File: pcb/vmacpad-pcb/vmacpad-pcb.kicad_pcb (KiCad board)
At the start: 2 copper layers, 134.7 x 126.1 mm, 79 parts, among them J1 TYPE-C-31-M12_13, J2 Conn_01x04_Pin, J3 Conn_01x04_Pin, K1 1u, K10 1u, K12 2.25u, K13 1u, K14 1u, K16 1u, K17 1u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

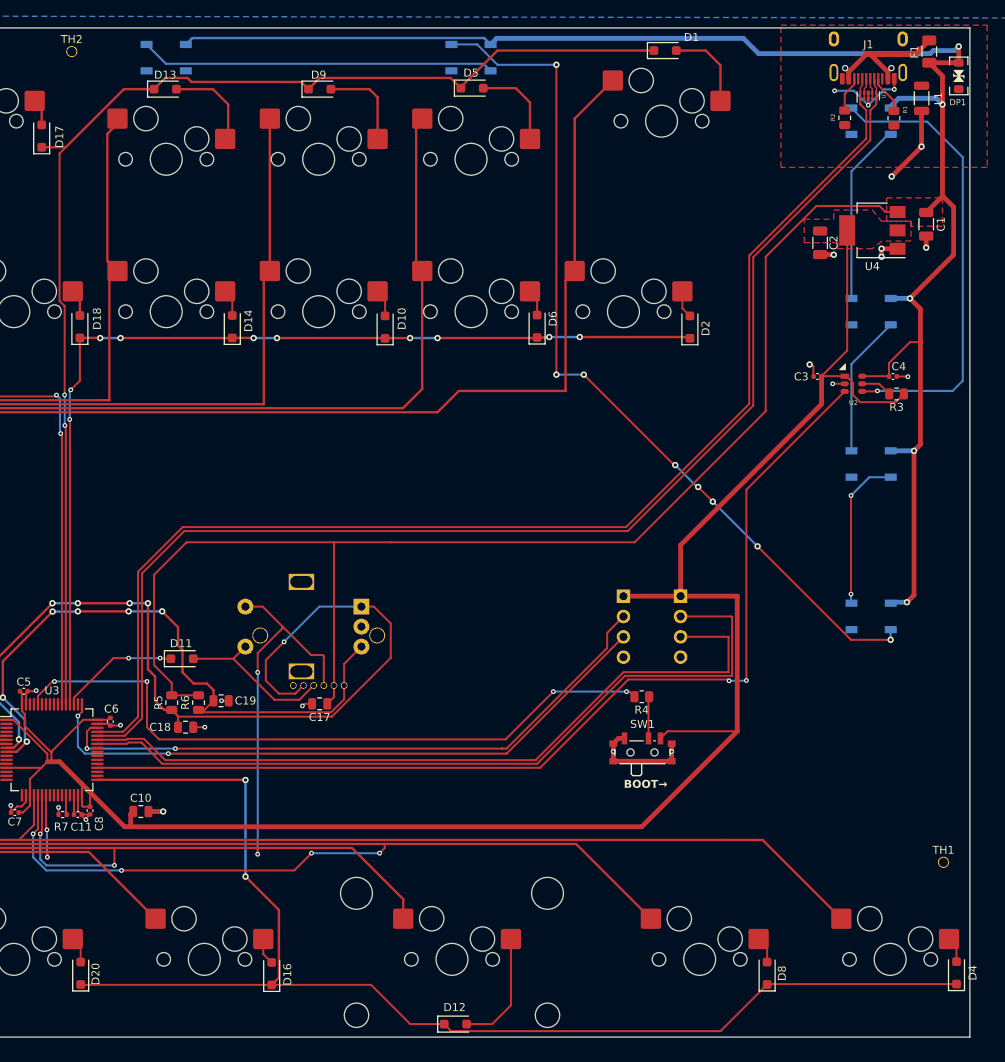
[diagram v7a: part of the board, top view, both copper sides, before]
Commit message: Fix power trace width
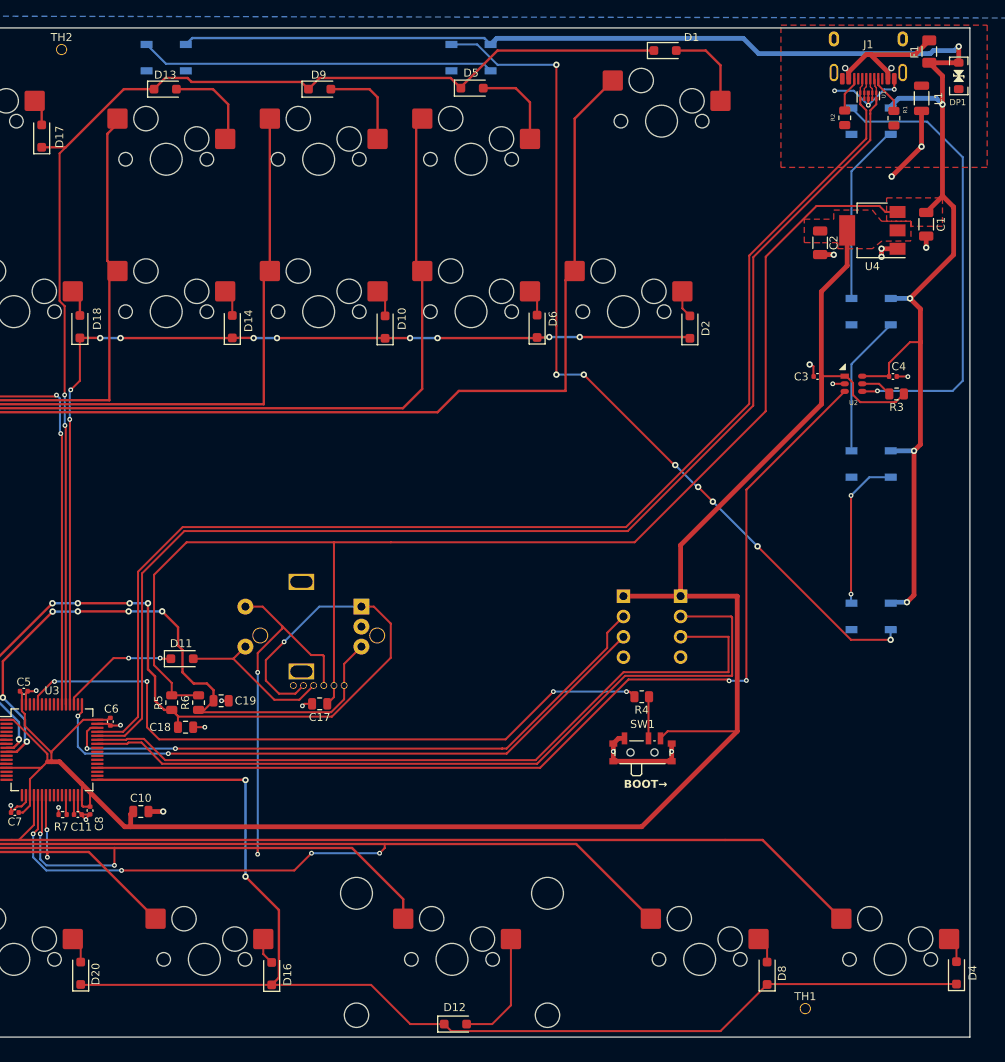
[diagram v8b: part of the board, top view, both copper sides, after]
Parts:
- moved TH1 25.2 mm to (203.7, 220.5)
- moved TH2 1.30 mm to (110.7, 100.6)
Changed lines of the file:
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@@
   )
   (footprint "max_customs:jlcpcb_tooling" (layer "F.Cu")
-    (at 112.014 100.838)
+    (at 110.744 100.584)
     (attr through_hole)
     (fp_text reference "TH2" (at 0 -1.524 unlocked) (layer "F.SilkS")
@@
   )
   (footprint "max_customs:jlcpcb_tooling" (layer "F.Cu")
-    (at 220.98 202.184)
+    (at 203.708 220.472)
     (attr through_hole)
     (fp_text reference "TH1" (at 0 -1.524 unlocked) (layer "F.SilkS")
@@
     (property "ki_keywords" "rotary switch encoder switch push button")
     (attr through_hole exclude_from_bom)
-    (fp_text reference "SW3" (at -5.461 7.53745) (layer "B.SilkS")
+    (fp_text reference "SW3" (at -5.715 7.71525) (layer "B.SilkS")
         (effects (font (size 1 1) (thickness 0.15)) (justify mirror))
     )
@@
         (effects (font (size 1 1) (thickness 0.15)) (justify mirror))
     )
-    (fp_text user "1" (at -4.15 1.6) (layer "B.SilkS")
+    (fp_text user "1" (at -4.15 1.27) (layer "B.SilkS")
         (effects (font (size 1 1) (thickness 0.15)) (justify mirror))
     )
@@
   (segment (start 208.6356 106.13148) (end 208.6356 108.2059) (width 0.254) (layer "F.Cu") (net 7))
   (segment (start 209.832 104.2355) (end 209.832 104.93508) (width 0.254) (layer "F.Cu") (net 7))
+  (segment (start 205.712 141.4526) (end 205.712 130.838) (width 0.6) (layer "F.Cu") (net 9))
   (segment (start 114.301144 193.419856) (end 113.221644 192.340356) (width 0.6) (layer "F.Cu") (net 9))
   (segment (start 113.2875 193.79375) (end 113.2875 192.406212) (width 0.254) (layer "F.Cu") (net 9))
@@
   (segment (start 188.11875 168.91) (end 195.199 168.91) (width 0.6) (layer "F.Cu") (net 9))
   (segment (start 209.677 143.764) (end 209.677 142.2593) (width 0.254) (layer "F.Cu") (net 9))
+  (segment (start 208.94 127.61) (end 208.94 123.19) (width 0.6) (layer "F.Cu") (net 9))
   (segment (start 105.7875 182.44375) (end 105.7875 181.0451) (width 0.254) (layer "F.Cu") (net 9))
   (segment (start 195.199 185.801) (end 183.261 197.739) (width 0.6) (layer "F.Cu") (net 9))
@@
   (segment (start 106.142236 185.136236) (end 109.4105 188.4045) (width 0.254) (layer "F.Cu") (net 9))
   (segment (start 208.8347 141.417) (end 208.6297 141.417) (width 0.254) (layer "F.Cu") (net 9))
-  (segment (start 205.7369 141.417) (end 205.7013 141.4526) (width 0.254) (layer "F.Cu") (net 9))
   (segment (start 210.577 144.664) (end 209.677 143.764) (width 0.254) (layer "F.Cu") (net 9))
   (segment (start 105.7875 183.287264) (end 106.142236 183.642) (width 0.254) (layer "F.Cu") (net 9))
@@
   (segment (start 109.4105 188.4045) (end 109.474 188.468) (width 0.254) (layer "F.Cu") (net 9))
   (segment (start 216.027 143.637) (end 215 144.664) (width 0.254) (layer "F.Cu") (net 9))
+  (segment (start 205.712 130.838) (end 208.94 127.61) (width 0.6) (layer "F.Cu") (net 9))
   (segment (start 114.3 195.227) (end 114.3 193.421) (width 0.254) (layer "F.Cu") (net 9))
   (segment (start 118.620288 197.739) (end 114.301144 193.419856) (width 0.6) (layer "F.Cu") (net 9))
-  (segment (start 208.94 138.2139) (end 208.94 123.19) (width 0.254) (layer "F.Cu") (net 9))
   (segment (start 103.8625 184.36875) (end 102.55275 184.36875) (width 0.254) (layer "F.Cu") (net 9))
-  (segment (start 205.7013 141.4526) (end 208.94 138.2139) (width 0.254) (layer "F.Cu") (net 9))
   (segment (start 116.49425 184.36875) (end 115.2125 184.36875) (width 0.254) (layer "F.Cu") (net 9))
   (segment (start 115.2125 184.36875) (end 113.44625 184.36875) (width 0.254) (layer "F.Cu") (net 9))
@@
     (connect_pads (clearance 0.254))
     (min_thickness 0.2032) (filled_areas_thickness no)
-    (fill yes (thermal_gap 0.254) (thermal_bridge_width 0.3048))
+    (fill yes (thermal_gap 0.254) (thermal_bridge_width 0.381))
     (polygon
       (pts
